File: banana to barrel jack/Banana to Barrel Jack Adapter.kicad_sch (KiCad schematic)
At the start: 11 parts, among them J1 USB_A, J2 Positive, J3 Negative, J4 Data

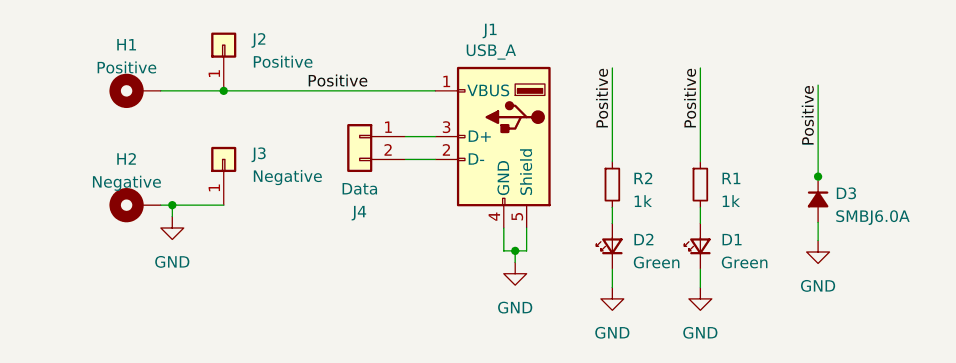
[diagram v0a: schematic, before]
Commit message: DRC is giving off-grid errors and "GND modified"
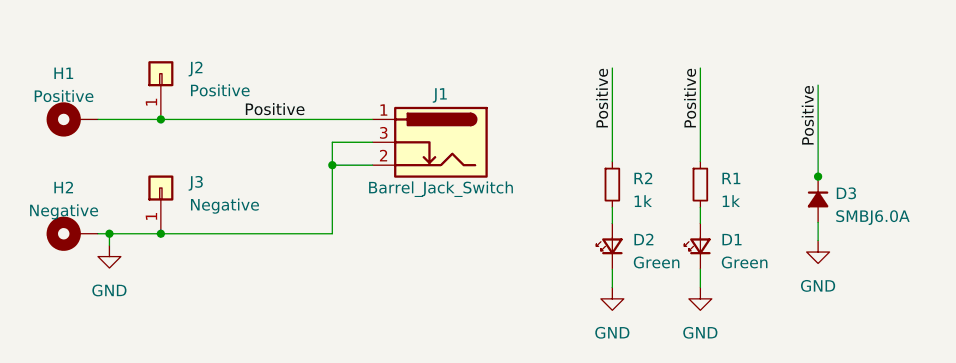
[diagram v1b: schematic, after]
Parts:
- removed J1: USB_A, My Libraries:USB_A_GCT_USB1125, symbol Connector:USB_A
- removed J4: Data, Connector_PinHeader_2.54mm:PinHeader_1x02_P2.54mm_Vertical, symbol Connector_Generic:Conn_01x02
- added J1: Barrel_Jack_Switch, Connector_BarrelJack:BarrelJack_GCT_DCJ200-10-A_Horizontal, symbol Connector:Barrel_Jack_Switch
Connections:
- net GND: now also J1.2, J1.3
- net Positive: now also J1.1
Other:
- moved on the sheet: H1, H2, J2, J3

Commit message: Cleared DRC issues
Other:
- moved on the sheet: D1, D2, D3, H1, H2, J1, J2, J3, R2
